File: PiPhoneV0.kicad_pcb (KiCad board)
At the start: 2 copper layers, 87 x 165 mm, 41 parts, among them J1 GPIO, SW1 SW_Push, SW10 SW_Push, SW11 SW_Push, SW12 SW_Push, SW13 SW_Push, SW14 SW_Push, SW15 SW_Push, SW16 SW_Push, SW17 SW_Push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

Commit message: feat: speaker
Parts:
- added C1: 100uf, Capacitor_THT:CP_Axial_L10.0mm_D4.5mm_P15.00mm_Horizontal, F.Cu at (160.7, 169.2)
- added C2: 100uf, Capacitor_THT:CP_Axial_L10.0mm_D4.5mm_P15.00mm_Horizontal, F.Cu at (160.7, 175.7)
- added C3: 100nf, Capacitor_THT:CP_Axial_L10.0mm_D4.5mm_P15.00mm_Horizontal, F.Cu at (160.7, 182.3)
- added C4: 1000uf, Capacitor_THT:CP_Axial_L10.0mm_D4.5mm_P15.00mm_Horizontal, F.Cu at (160.7, 188.8)
- added IC1: LM386M-1_NOPB, LM386M-1_NOBP:SOIC127P600X175-8N, F.Cu at (178.3, 195.9)
- added LS1: Speaker, Buzzer_Beeper:Speaker_CUI_CMR-1206S-67, F.Cu at (165.4, 196.4)
- added R3: 10k, Resistor_SMD:R_0201_0603Metric, F.Cu at (186.7, 174.9)
- D1, D10, D11, D12, D13, D14, D15, D16, D17, D18, D2, D3, D4, D5, D6, D7, D8, D9: footprint Diode_SMD:D_0201_0603Metric -> Diode_THT:D_5KPW_P12.70mm_Horizontal

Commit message: chore: flip pcb
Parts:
- moved J1 67.1 mm to (156.6, 95.4), turned to 90 degrees
- moved R3 17.1 mm to (178.7, 190.0)
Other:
- outline, holes or cut-outs redrawn
- board text removed: "DISPLAY (OPTIONAL)"

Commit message: chore: body curve
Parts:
- removed MH1, MH2: MountingHole_2.7mm_M2.5, MountingHole:MountingHole_2.7mm_M2.5
- C1, C4: footprint Capacitor_THT:CP_Axial_L10.0mm_D4.5mm_P15.00mm_Horizontal -> Capacitor_SMD:CP_Elec_3x5.3
- C2, C3: footprint Capacitor_THT:CP_Axial_L10.0mm_D4.5mm_P15.00mm_Horizontal -> Capacitor_SMD:C_0201_0603Metric
- D1, D10, D11, D12, D13, D14, D15, D16, D17, D18, D2, D3, D4, D5, D6, D7, D8, D9: footprint Diode_THT:D_5KPW_P12.70mm_Horizontal -> Diode_SMD:D_0201_0603Metric
- R3: footprint Resistor_SMD:R_0201_0603Metric -> Diode_SMD:D_0201_0603Metric
- moved R3 33.1 mm to (145.8, 194.5)
- moved C2 27.2 mm to (145.8, 198.5)
- moved IC1 26.3 mm to (152.2, 192.4)
- moved LS1 20.1 mm to (154.5, 179.5), turned to -90 degrees
- moved C3 16.5 mm to (145.8, 189.5)
- moved C1 15.9 mm to (146.5, 176.5)
- moved C4 15.1 mm to (146.5, 183.5)
- moved D1 13.7 mm to (107.7, 134.5)
- moved D15 13.7 mm to (107.7, 166.5)
- moved D5 13.7 mm to (107.7, 182.5)
- moved D6 13.7 mm to (107.7, 198.5)
- moved D8 13.7 mm to (107.7, 150.5)
- moved SW1 13.7 mm to (102.6, 131.5)
- moved SW10 13.7 mm to (118.6, 163.5)
- moved SW13 13.7 mm to (102.6, 179.5)
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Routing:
- net /GPIO27: track 234.7 -> 155.9 mm
- net /GPIO16: track 145.7 -> 74.6 mm
- net /GPIO19/PCM.FS: track 114.6 -> 78.7 mm
- net /GPIO17: track 159.2 -> 148.2 mm
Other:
- board size 87 x 165 mm -> 70.5 x 117.5 mm
- board text removed: "RJ45"
- board text removed: "USB"

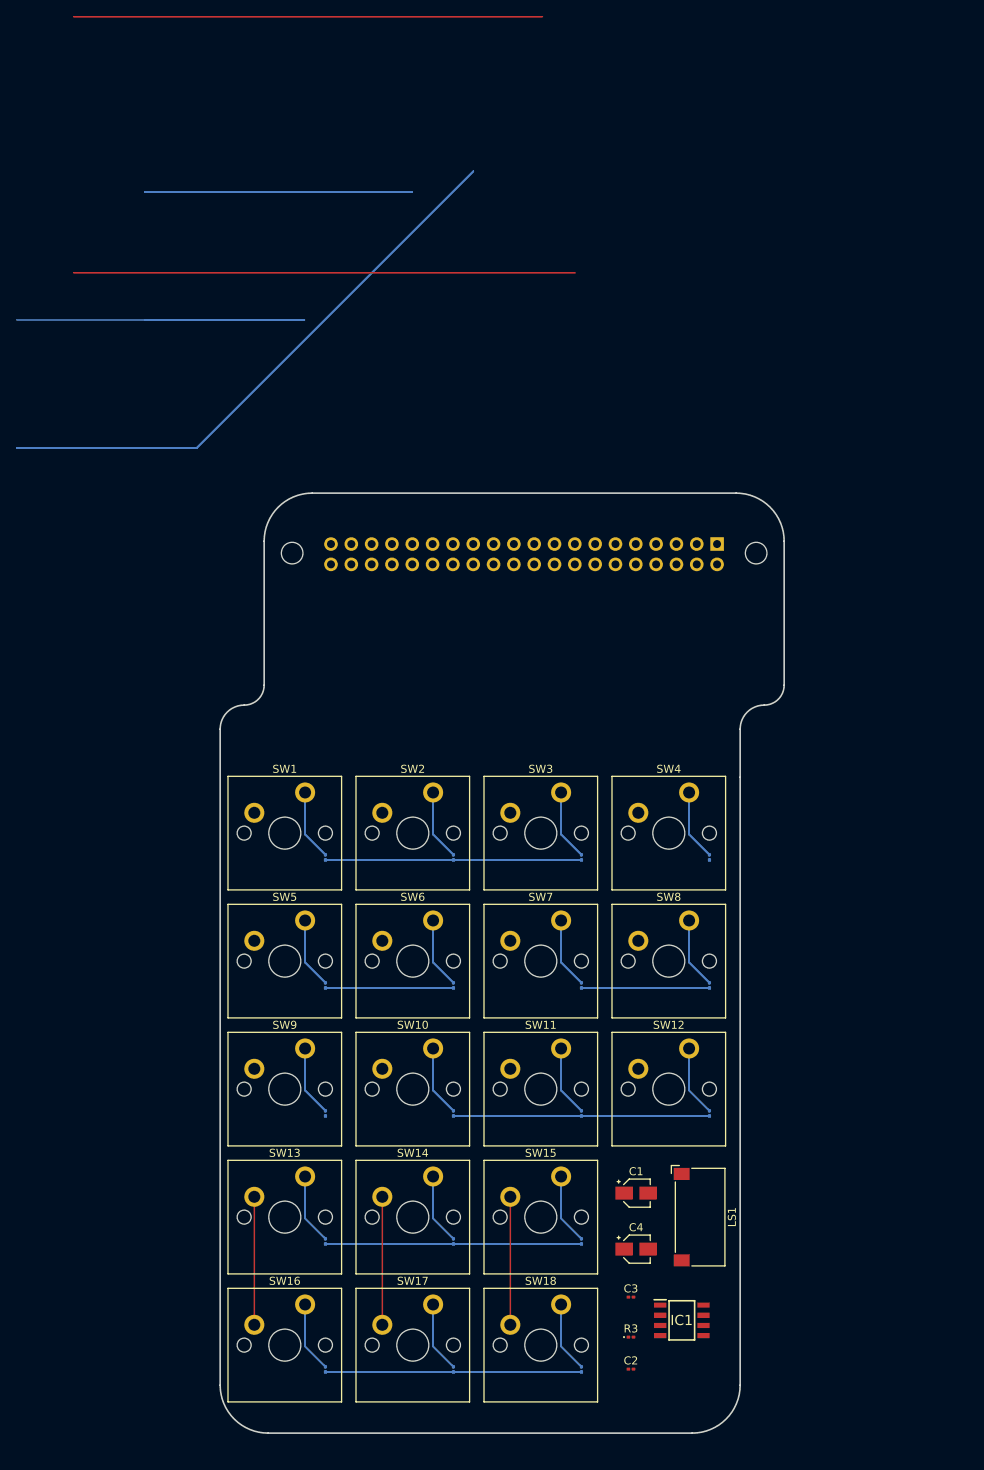
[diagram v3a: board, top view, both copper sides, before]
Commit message: fix: switch key switches for low profile
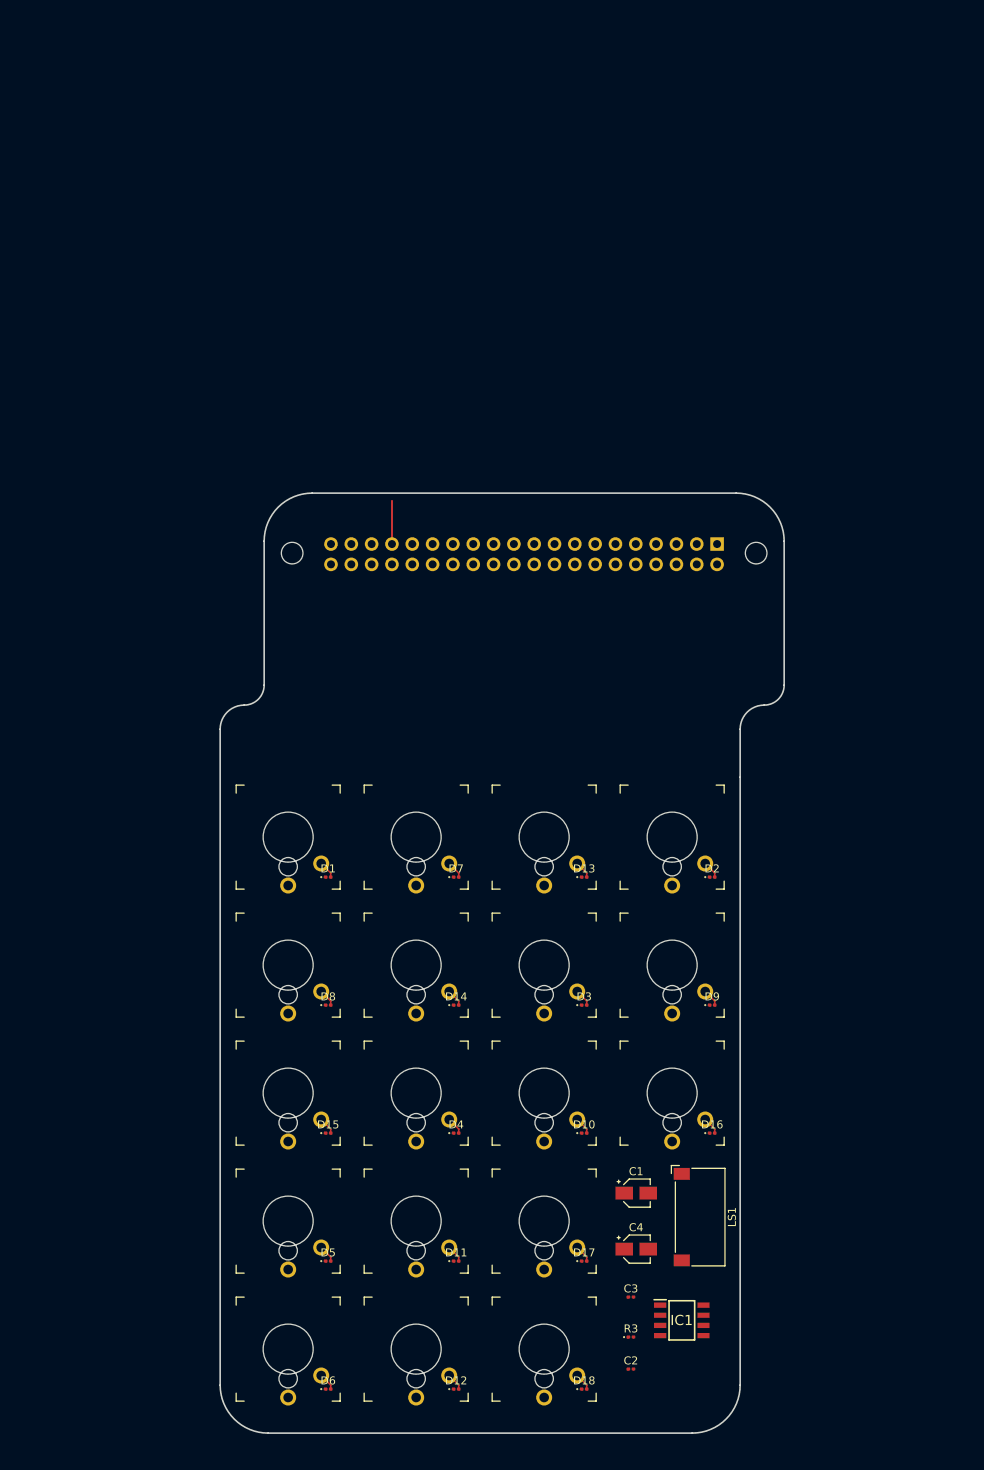
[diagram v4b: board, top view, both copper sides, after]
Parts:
- D1, D10, D11, D12, D13, D14, D15, D16, D17, D18, D2, D3, D4, D5, D6, D7, D8, D9: moved to F.Cu
- SW1, SW10, SW11, SW12, SW13, SW14, SW15, SW16, SW17, SW18, SW2, SW3, SW4, SW5, SW6, SW7, SW8, SW9: footprint PCM_Switch_Keyboard_Cherry_MX:SW_Cherry_MX_PCB -> 1 key-switches.pretty:SW_MX_LowProfile_THT
- moved D1 2.49 mm to (108.0, 137.0), turned to 0 degrees
- moved D10 2.49 mm to (140.0, 169.0), turned to 0 degrees
- moved D11 2.49 mm to (124.0, 185.0), turned to 0 degrees
- moved D12 2.49 mm to (124.0, 201.0), turned to 0 degrees
- moved D13 2.49 mm to (140.0, 137.0), turned to 0 degrees
- moved D14 2.49 mm to (124.0, 153.0), turned to 0 degrees
- moved D15 2.49 mm to (108.0, 169.0), turned to 0 degrees
- moved D16 2.49 mm to (156.0, 169.0), turned to 0 degrees
- moved D17 2.49 mm to (140.0, 185.0), turned to 0 degrees
- moved D18 2.49 mm to (140.0, 201.0), turned to 0 degrees
- moved D2 2.49 mm to (156.0, 137.0), turned to 0 degrees
- moved D3 2.49 mm to (140.0, 153.0), turned to 0 degrees
- moved D4 2.49 mm to (124.0, 169.0), turned to 0 degrees
- moved D5 2.49 mm to (108.0, 185.0), turned to 0 degrees
- moved D6 2.49 mm to (108.0, 201.0), turned to 0 degrees
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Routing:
- net /GPIO22: track 294.2 -> 0.00 mm
- net /GPIO27: track 155.9 -> 0.00 mm
- net /GPIO17: track 148.2 -> 0.00 mm
- net /GPIO5: track 96.0 -> 0.00 mm
- net /GPIO23: track 80.0 -> 0.00 mm
- net /GPIO19/PCM.FS: track 78.7 -> 0.00 mm
- net /GPIO16: track 74.6 -> 0.00 mm
- net /GPIO6: track 48.0 -> 0.00 mm
- net Net-(D9-A): track 26.5 -> 2.19 mm
- net Net-(D4-A): track 26.5 -> 2.19 mm
- net Net-(D3-A): track 26.5 -> 2.19 mm
- net Net-(D15-A): track 26.5 -> 2.19 mm
- net Net-(D14-A): track 26.5 -> 2.19 mm
- net Net-(D10-A): track 26.5 -> 2.19 mm
- net Net-(D8-A): track 26.5 -> 2.19 mm
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
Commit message: feat: routing
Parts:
- removed C1: 100uf, Capacitor_SMD:CP_Elec_3x5.3
- removed C2: 100uf, Capacitor_SMD:C_0201_0603Metric
- removed C3: 100nf, Capacitor_SMD:C_0201_0603Metric
- removed C4: 1000uf, Capacitor_SMD:CP_Elec_3x5.3
- removed IC1: LM386M-1_NOPB, LM386M-1_NOBP:SOIC127P600X175-8N
- removed LS1: Speaker, Buzzer_Beeper:Speaker_CUI_CMR-1206S-67
- removed R3: 10k, Diode_SMD:D_0201_0603Metric
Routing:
- net /GPIO19/PCM.FS: track 0.00 -> 284.6 mm
- net /GPIO13/PWM1: track 21.4 -> 238.5 mm
- net /GPIO16: track 0.00 -> 196.9 mm
- net /GPIO23: track 0.00 -> 175.1 mm
- net /GPIO22: track 0.00 -> 154.0 mm
- net /GPIO17: track 0.00 -> 133.9 mm
- net /GPIO27: track 0.00 -> 127.0 mm
- net /GPIO5: track 0.00 -> 125.6 mm
- net /GPIO6: track 0.00 -> 112.9 mm

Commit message: wip: backlight
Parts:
- added J2: TL040WVS03-H1263A, Connector_FFC-FPC:Hirose_FH12-40S-0.5SH_1x40-1MP_P0.50mm_Horizontal, F.Cu at (119.2, 109.2)
- added J3: Conn_01x15_MountingPin, Connector_FFC-FPC:Molex_200528-0150_1x15-1MP_P1.00mm_Horizontal, F.Cu at (145.9, 118.6)
- added U1: ~, Package_DFN_QFN:QFN-48-1EP_6x6mm_P0.4mm_EP4.2x4.2mm, F.Cu at (124.3, 118.4)
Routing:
- net /GPIO5: track 125.6 -> 171.1 mm
- net Net-(J3-Pin_11): track 0.00 -> 39.0 mm
- net /GPIO6: track 112.9 -> 129.2 mm
- net /GPIO19/PCM.FS: track 284.6 -> 298.7 mm
- net /GPIO16: track 196.9 -> 205.2 mm
- net /GPIO13/PWM1: track 238.5 -> 242.4 mm
- net +3V3: track 0.00 -> 0.57 mm

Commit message: feat: screen
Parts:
- added C5: 220 nF, Capacitor_SMD:C_0201_0603Metric, B.Cu at (139.1, 104.3)
- added C6: 1uF, Capacitor_SMD:C_0201_0603Metric, B.Cu at (139.1, 106.1)
- added C7: 1uF, Capacitor_SMD:C_0201_0603Metric, B.Cu at (139.1, 107.8)
- added D20: MBR0540, Diode_SMD:D_SOD-123, B.Cu at (145.9, 113.0)
- added L1: 22uH, Inductor_SMD:L_6.3x6.3_H3, B.Cu at (144.6, 107.4)
- added R1: 5, Resistor_SMD:R_0201_0603Metric, B.Cu at (139.1, 109.6)
- added U2: TPS61165DRV, Package_SON:WSON-6-1EP_2x2mm_P0.65mm_EP1x1.6mm, B.Cu at (141.0, 113.2)
- U1: moved to B.Cu
- moved U1 28.3 mm to (152.6, 118.6), turned to 180 degrees
- moved J3 24.6 mm to (121.4, 117.6), turned to 180 degrees
- moved J2 5.47 mm to (123.7, 106.2)
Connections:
- J2 pad 1: unconnected-(J2-LED_A-Pad1) -> Net-(D20-K)
- J2 pad 2: unconnected-(J2-LED_K1-Pad2) -> Net-(J2-LED_K1)
- J2 pad 3: unconnected-(J2-LED_K2-Pad3) -> Net-(J2-LED_K1)
- J2 pad 5: +3V3 -> Net-(J2-VCI)
- J2 pad 6: unconnected-(J2-RESET-Pad6) -> /GPIO24
- U1 pad 11: unconnected-(U1-EN-Pad11) -> /GPIO25
- U1 pad 24: unconnected-(U1-VDD2-Pad24) -> +3V3
- U1 pad 3: unconnected-(U1-VDD3-Pad3) -> Net-(J2-VCI)
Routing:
- net GND: track 0.00 -> 101.6 mm, vias 0 -> 4
- net Net-(J2-PCLK): track 0.00 -> 62.6 mm, vias 0 -> 1
- net Net-(J2-HSYNC): track 0.00 -> 58.8 mm, vias 0 -> 1
- net Net-(J2-VSYNC): track 0.00 -> 58.4 mm, vias 0 -> 1
- net Net-(J2-DE): track 0.00 -> 58.1 mm, vias 0 -> 1
- net Net-(J2-DB6): track 0.00 -> 51.3 mm, vias 0 -> 1
- net Net-(J2-DB7): track 0.00 -> 50.6 mm, vias 0 -> 1
- net Net-(J2-DB8): track 0.00 -> 50.1 mm, vias 0 -> 1
- net Net-(J3-Pin_12): track 0.00 -> 50.1 mm, vias 0 -> 1
- net Net-(J2-DB0): track 0.00 -> 46.8 mm, vias 0 -> 1
- net Net-(J3-Pin_14): track 0.00 -> 46.6 mm, vias 0 -> 1
- net Net-(J2-DB1): track 0.00 -> 46.2 mm, vias 0 -> 1
- net Net-(J2-DB2): track 0.00 -> 45.5 mm, vias 0 -> 1
- net /GPIO25: track 0.00 -> 44.7 mm, vias 0 -> 2
- net Net-(J2-DB3): track 0.00 -> 43.9 mm, vias 0 -> 1
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
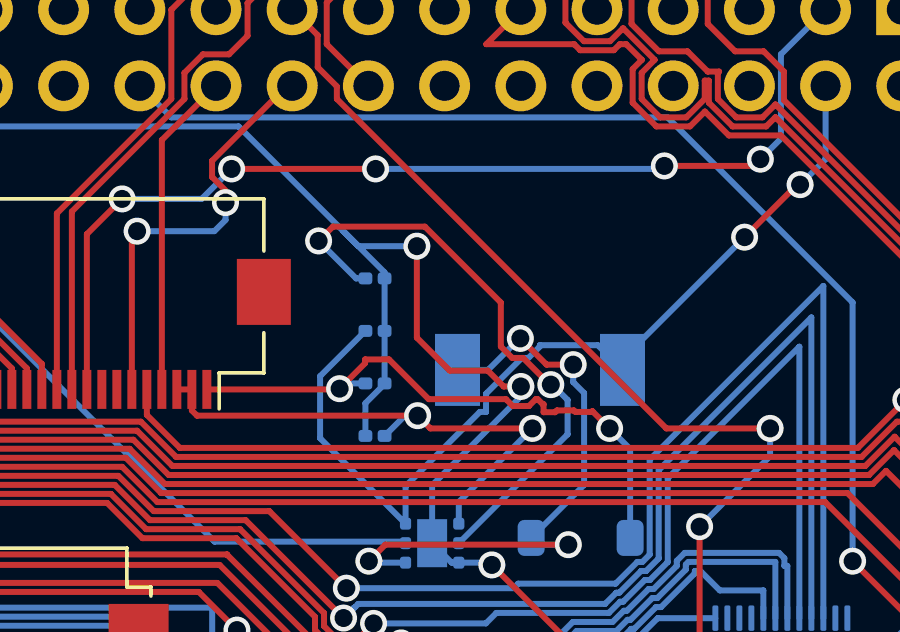
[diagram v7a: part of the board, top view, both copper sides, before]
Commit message: feat: protect backlight led
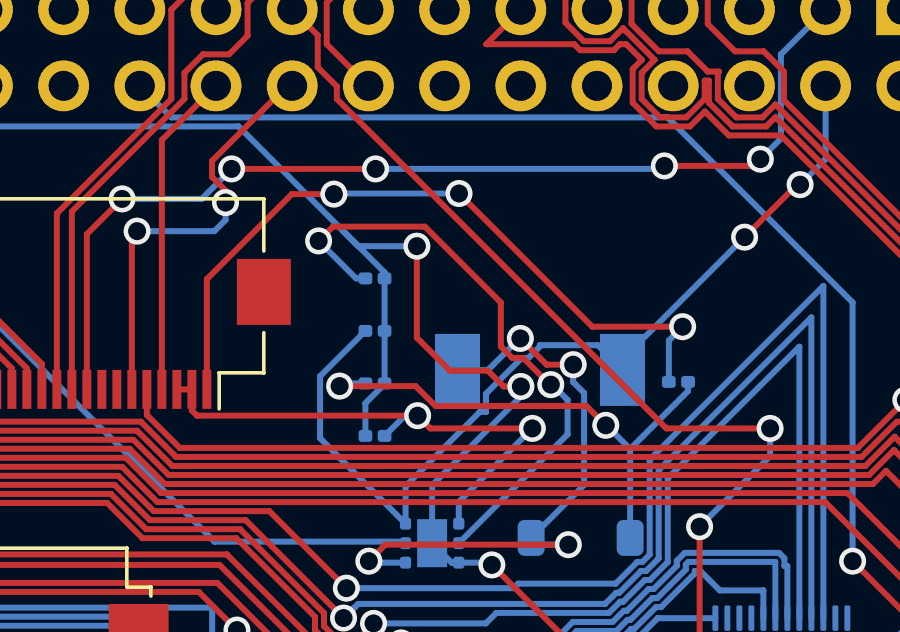
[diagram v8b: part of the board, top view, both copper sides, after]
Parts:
- added R2: 320, Resistor_SMD:R_0201_0603Metric, B.Cu at (149.2, 107.8)
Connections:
- J2 pad 1: Net-(D20-K) -> Net-(J2-LED_A)
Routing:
- net Net-(J2-LED_A): track 0.00 -> 24.6 mm, vias 0 -> 3
- net Net-(D20-K): track 20.1 -> 17.4 mm
